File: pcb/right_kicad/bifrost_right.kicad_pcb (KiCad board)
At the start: 2 copper layers, 142.9 x 80.3 mm, 65 parts, among them J1 HRO_TYPE-C-31-M-12, J2 Conn_01x02, J3 Conn_01x06, J4 Conn_01x05, Q1 AO3401A, Q2 2N7002, Q3 AO3401A, SW1 SW_Push, SW10 SW_Push, SW11 SW_Push, SW12 SW_Push, SW13 SW_Push, SW14 SW_Push, SW15 SW_Push, SW16 SW_Push, SW17 SW_Push, SW18 SW_Push, SW19 SW_Push, SW2 SW_Push, SW20 SW_Push, SW21 SW_Push, SW22 SW_Push, SW23 SW_Push, SW3 SW_Push, SW4 SW_Push, SW5 SW_Push, SW6 SW_Push, SW7 SW_Push, SW8 SW_Push, SW9 SW_Push, T1 TS24CA, U1 MDBT50Q-1MV2, U2 TP4057, U3 SRV05-4, X1 32.768kHz

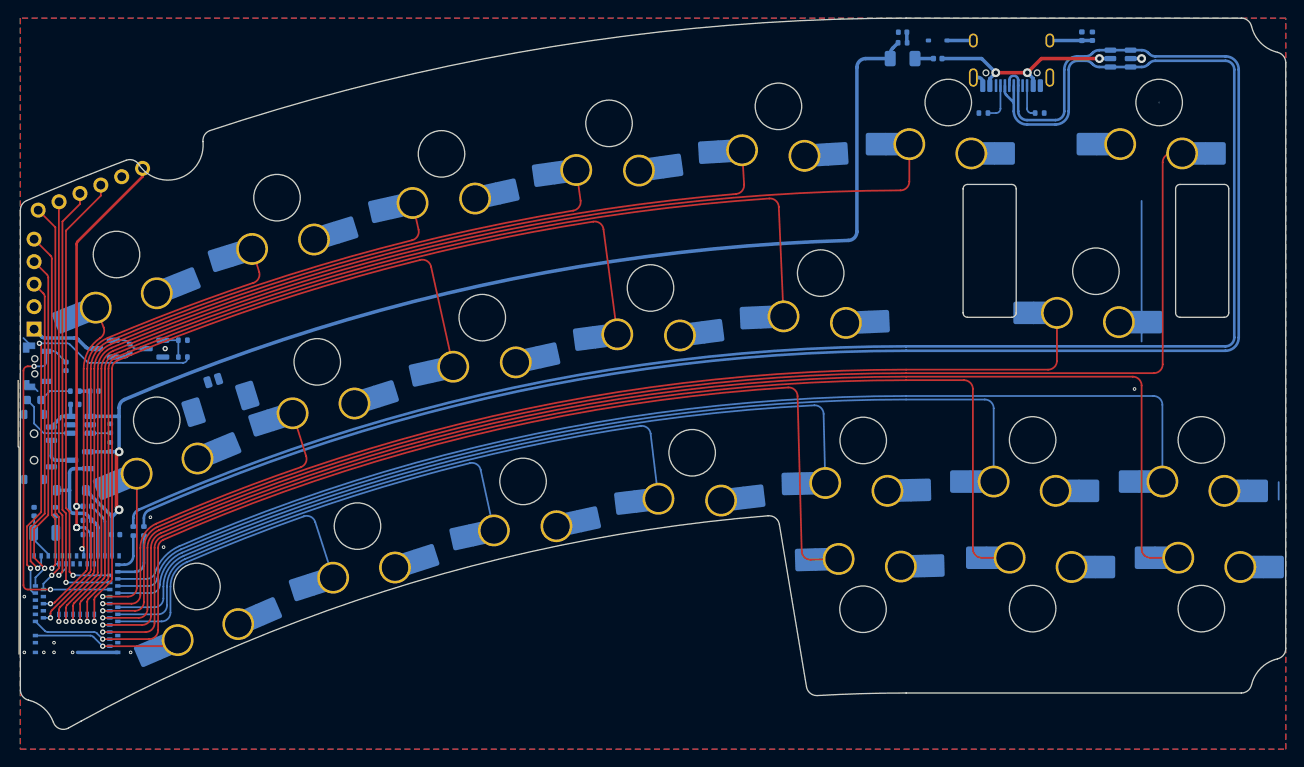
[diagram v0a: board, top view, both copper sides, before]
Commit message: Update KiCad keyboard designs
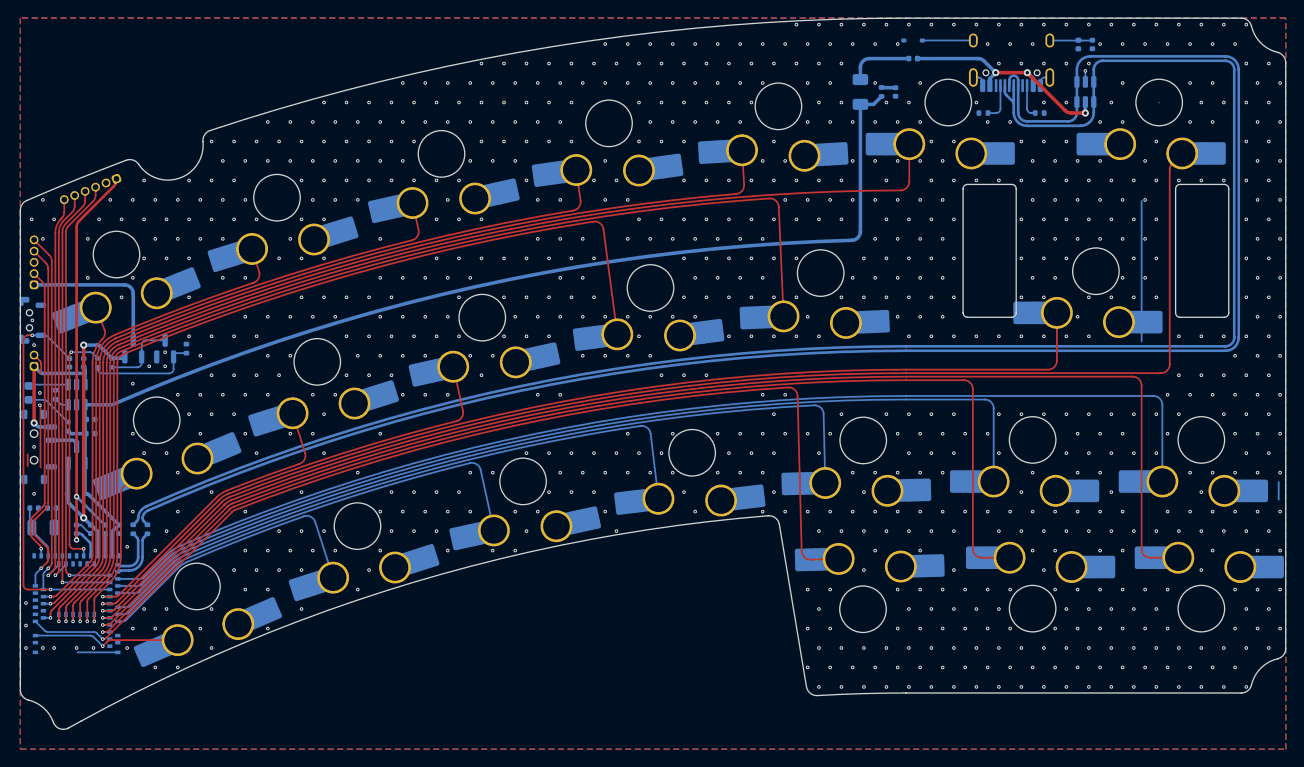
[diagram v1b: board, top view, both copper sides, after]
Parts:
- D2: value 1N5819W -> 1N5819WS; footprint Diode_SMD:D_SOD-123 -> Diode_SMD:D_SOD-323
- J2: footprint Connector_Molex:Molex_PicoBlade_53398-0271_1x02-1MP_P1.25mm_Vertical -> Connector_PinHeader_1.27mm:PinHeader_1x02_P1.27mm_Vertical
- J3: footprint Connector_PinHeader_2.54mm:PinHeader_1x06_P2.54mm_Vertical -> Connector_PinHeader_1.27mm:PinHeader_1x06_P1.27mm_Vertical
- J4: footprint Connector_PinHeader_2.54mm:PinHeader_1x05_P2.54mm_Vertical -> Connector_PinHeader_1.27mm:PinHeader_1x05_P1.27mm_Vertical
- moved J2 20.8 mm to (-131.8, 29.8), turned to 0 degrees
- moved R9 9.62 mm to (-124.6, 29.4), turned to -90 degrees
- moved R6 7.27 mm to (-129.4, 33.0)
- moved C10 6.79 mm to (-34.5, -1.19), turned to -90 degrees
- moved F1 6.07 mm to (-38.5, -1.19), turned to -90 degrees
- moved R7 6.04 mm to (-36.1, -1.19), turned to -90 degrees
- moved U3 5.47 mm to (-13.1, -1.19), turned to -90 degrees
- moved T1 5.23 mm to (-132.0, 24.6)
- moved J4 5.00 mm to (-131.8, 20.6)
- moved C9 4.81 mm to (-126.2, 29.4), turned to 90 degrees
- moved R3 4.08 mm to (-128.0, 36.6), turned to 90 degrees
- moved U2 3.42 mm to (-127.0, 33.0), turned to -90 degrees
- moved L1 3.28 mm to (-123.8, 48.2), turned to -90 degrees
- moved C7 3.22 mm to (-125.4, 35.8)
- moved Q3 3.20 mm to (-120.6, 27.8), turned to 90 degrees
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- renumbered LED1 to CHG1
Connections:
- J2 pad 1: GND -> +BATT
- J2 pad 2: +BATT -> GND
- J4 pad 2: GND -> RGB
- J4 pad 3: RGB -> GND
- T1 pad 1: /nRESET -> GND
- T1 pad 2: GND -> /nRESET
- U1 pad 11: unconnected-(U1-P0.02-Pad11) -> PIN_1
- U1 pad 12: RGB_EN -> unconnected-(U1-P0.31-Pad12)
- U1 pad 13: MOTION -> PIN_T2
- U1 pad 19: PIN_T2 -> MOTION
- U1 pad 26: PIN_1 -> RGB_EN
- U1 pad 42: PIN_2 -> PIN_5
- U1 pad 43: PIN_5 -> PIN_8
- U1 pad 61: PIN_8 -> PIN_2
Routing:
- net PIN_8: track 80.5 -> 53.7 mm
- net RGB_EN: track 47.4 -> 27.7 mm
- net +VSW: track 17.4 -> 36.7 mm, vias 0 -> 2
- net +5V: track 144.0 -> 129.0 mm, vias 2 -> 0
- net +BATT: track 3.98 -> 16.6 mm, vias 0 -> 1
- net GND: track 9.63 -> 20.6 mm, vias 12 -> 902
- net RGB_PWR: track 7.90 -> 17.0 mm
- net Net-(Q2-G): track 3.65 -> 12.5 mm
- net PIN_1: track 29.1 -> 36.2 mm
- net Net-(F1-Pad1): track 2.08 -> 7.37 mm
- net PIN_16: track 122.2 -> 117.2 mm
- net PIN_20: track 134.6 -> 129.8 mm
- net Earth: track 9.53 -> 14.1 mm
- net Net-(Q2-D): track 4.07 -> 8.58 mm
- net PIN_23: track 153.4 -> 149.0 mm
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
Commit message: Update PCB designs
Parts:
- SW1, SW10, SW11, SW12, SW13, SW14, SW15, SW16, SW17, SW19, SW2, SW20, SW22, SW23, SW3, SW4, SW5, SW6, SW7, SW8, SW9: value SW_Push -> 1U
- SW18: value SW_Push -> 2.25U
- SW21: value SW_Push -> 1.5U

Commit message: Update PCB and case designs
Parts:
- moved C1 211.7 mm to (77.8, 107.7)
- moved C2 211.7 mm to (76.2, 107.7)
- moved C3 211.7 mm to (81.0, 107.7)
- moved C5 211.7 mm to (71.4, 105.3)
- moved C6 211.7 mm to (73.4, 105.3)
- moved C7 211.7 mm to (77.8, 95.3)
- moved C9 211.7 mm to (77.0, 88.9)
- moved CHG1 211.7 mm to (70.8, 92.3)
- moved D1 211.7 mm to (170.7, 52.5)
- moved D2 211.7 mm to (76.2, 103.7)
- moved J1 211.7 mm to (181.8, 53.6)
- moved J2 211.7 mm to (71.4, 89.3)
- moved J3 211.7 mm to (80.7, 68.1)
- moved J4 211.7 mm to (71.4, 80.1)
- moved L2 211.7 mm to (189.3, 53.0)
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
